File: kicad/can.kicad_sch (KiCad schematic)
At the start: 8 parts, among them U4 TJA1051TK_3,118, U5 MCP2515T-E_ST, Y1 LFXTAL050985

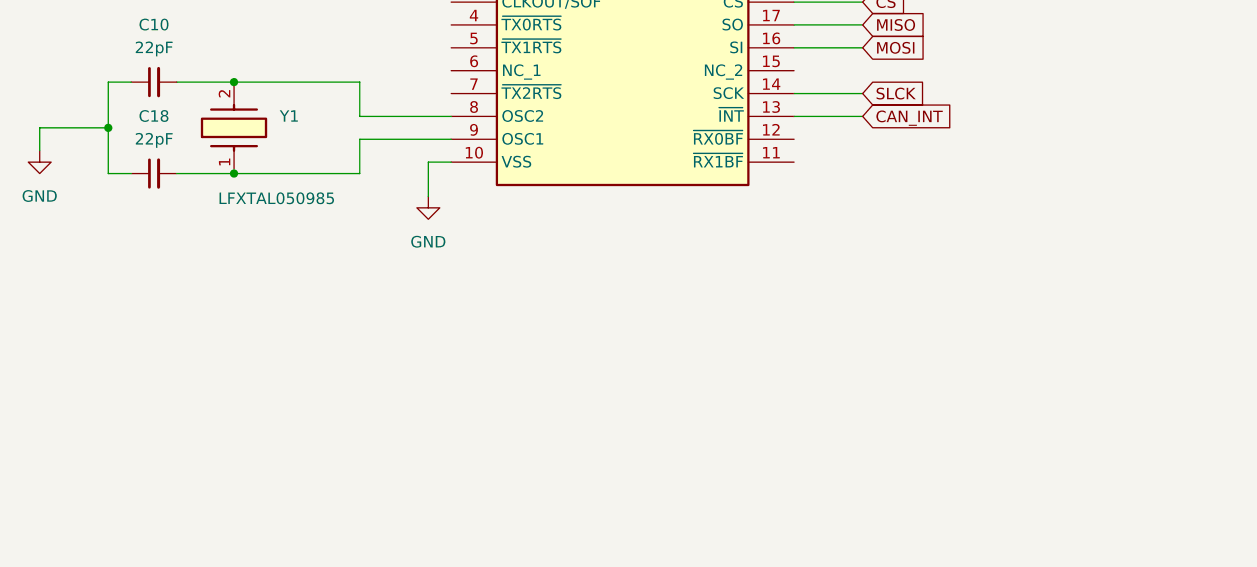
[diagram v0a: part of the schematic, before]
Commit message: Added PDF version of schematic
* Added comment in schematic regarding CAN bitrate
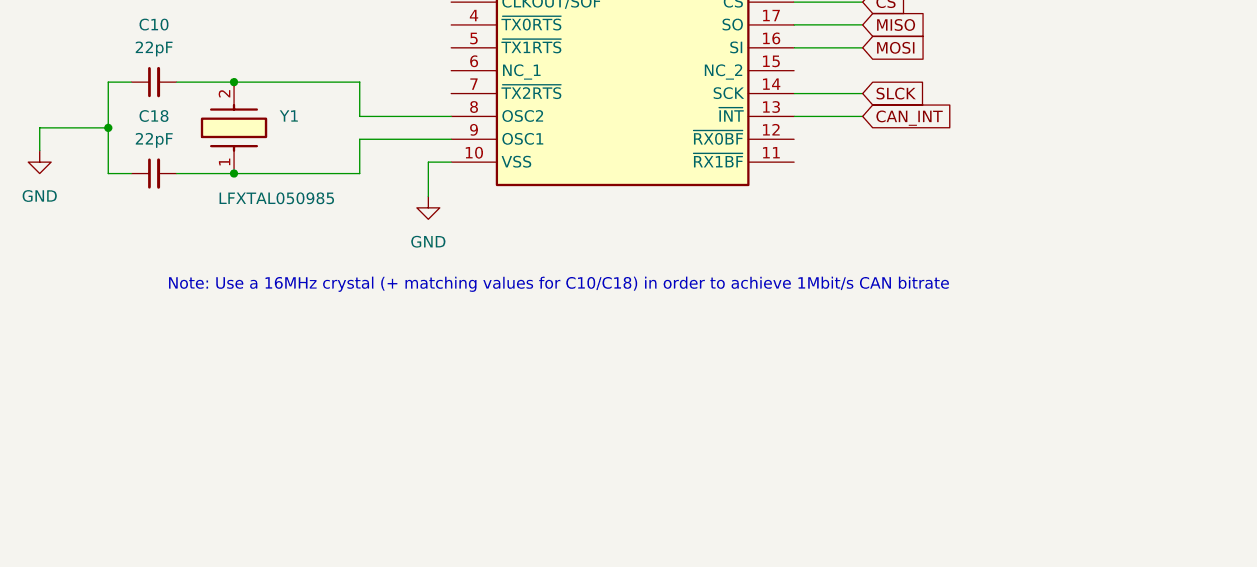
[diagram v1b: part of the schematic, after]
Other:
- note added: "Note: Use a 16MHz crystal (+ matching values for C10/C18) in order to achieve 1Mbit/s CAN bitrate"
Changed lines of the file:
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@@
+		)
+	)
+	(text "Note: Use a 16MHz crystal (+ matching values for C10/C18) in order to achieve 1Mbit/s CAN bitrate "
+		(exclude_from_sim no)
+		(at 132.588 121.666 0)
+		(effects
+			(font
+				(size 1.27 1.27)
+			)
 		)
 	)
